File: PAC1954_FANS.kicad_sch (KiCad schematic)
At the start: 11 parts, among them U25 PAC1954T-E_4MX

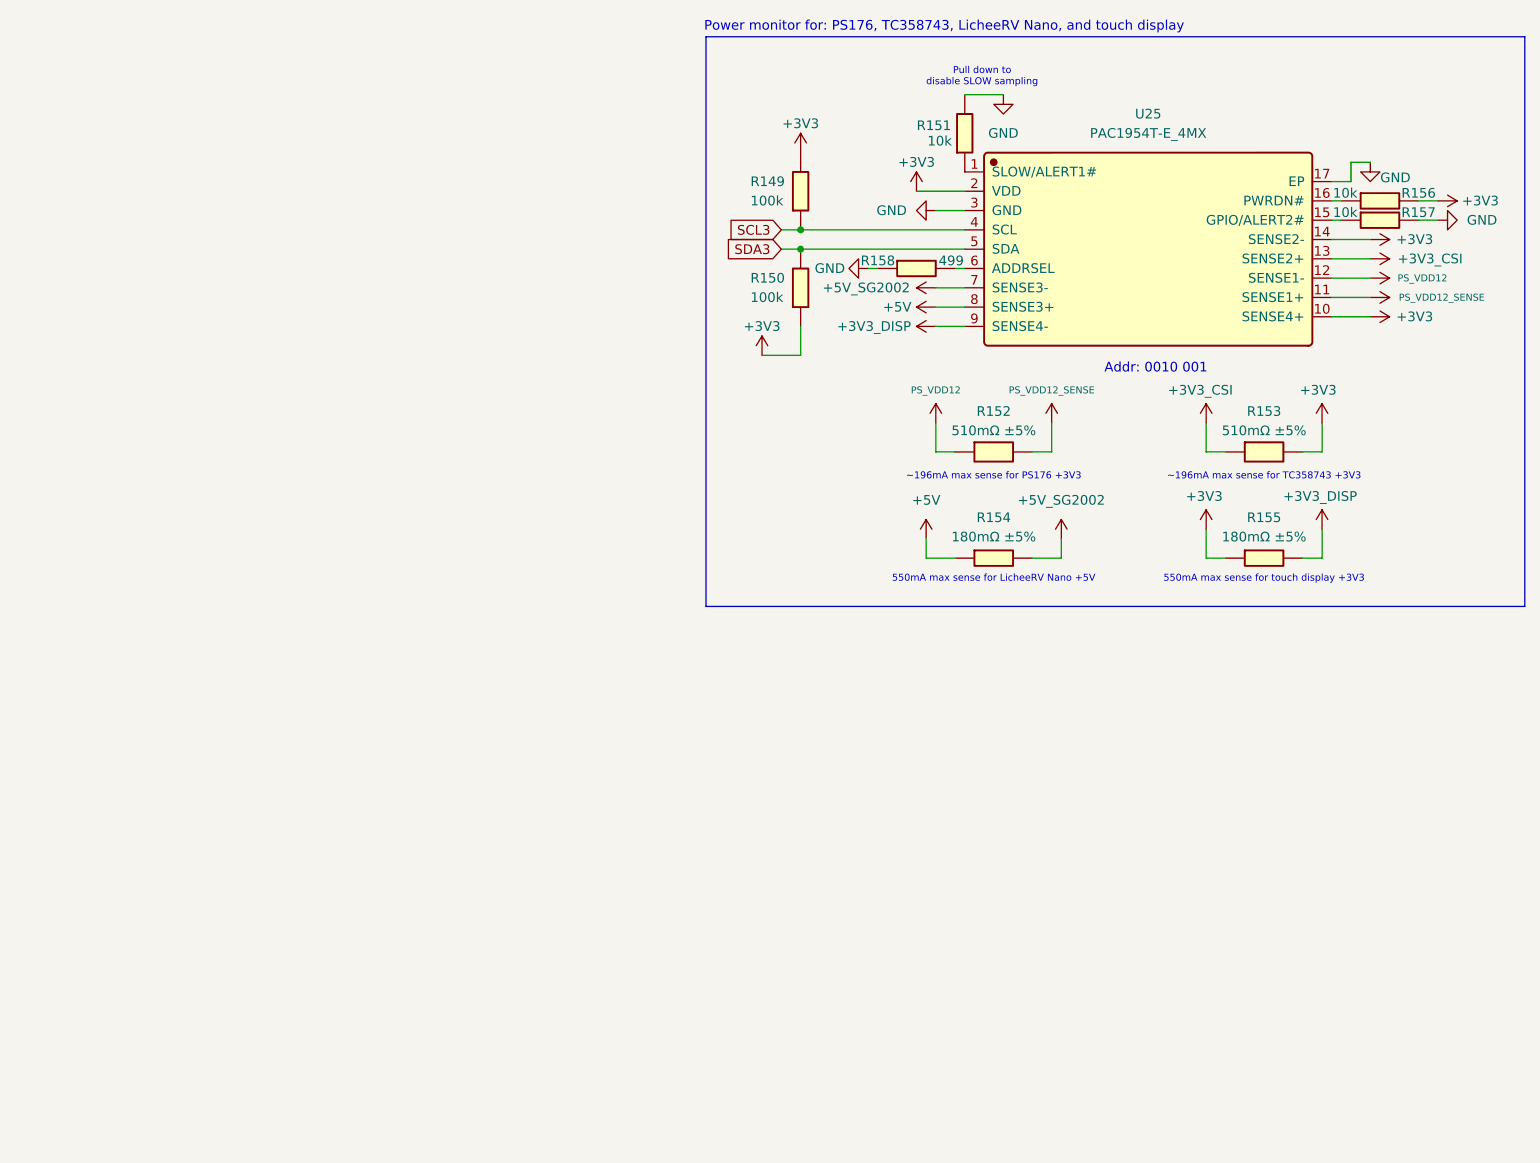
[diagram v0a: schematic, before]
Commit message: Mostly complete initial transfer to hierarchical schematic
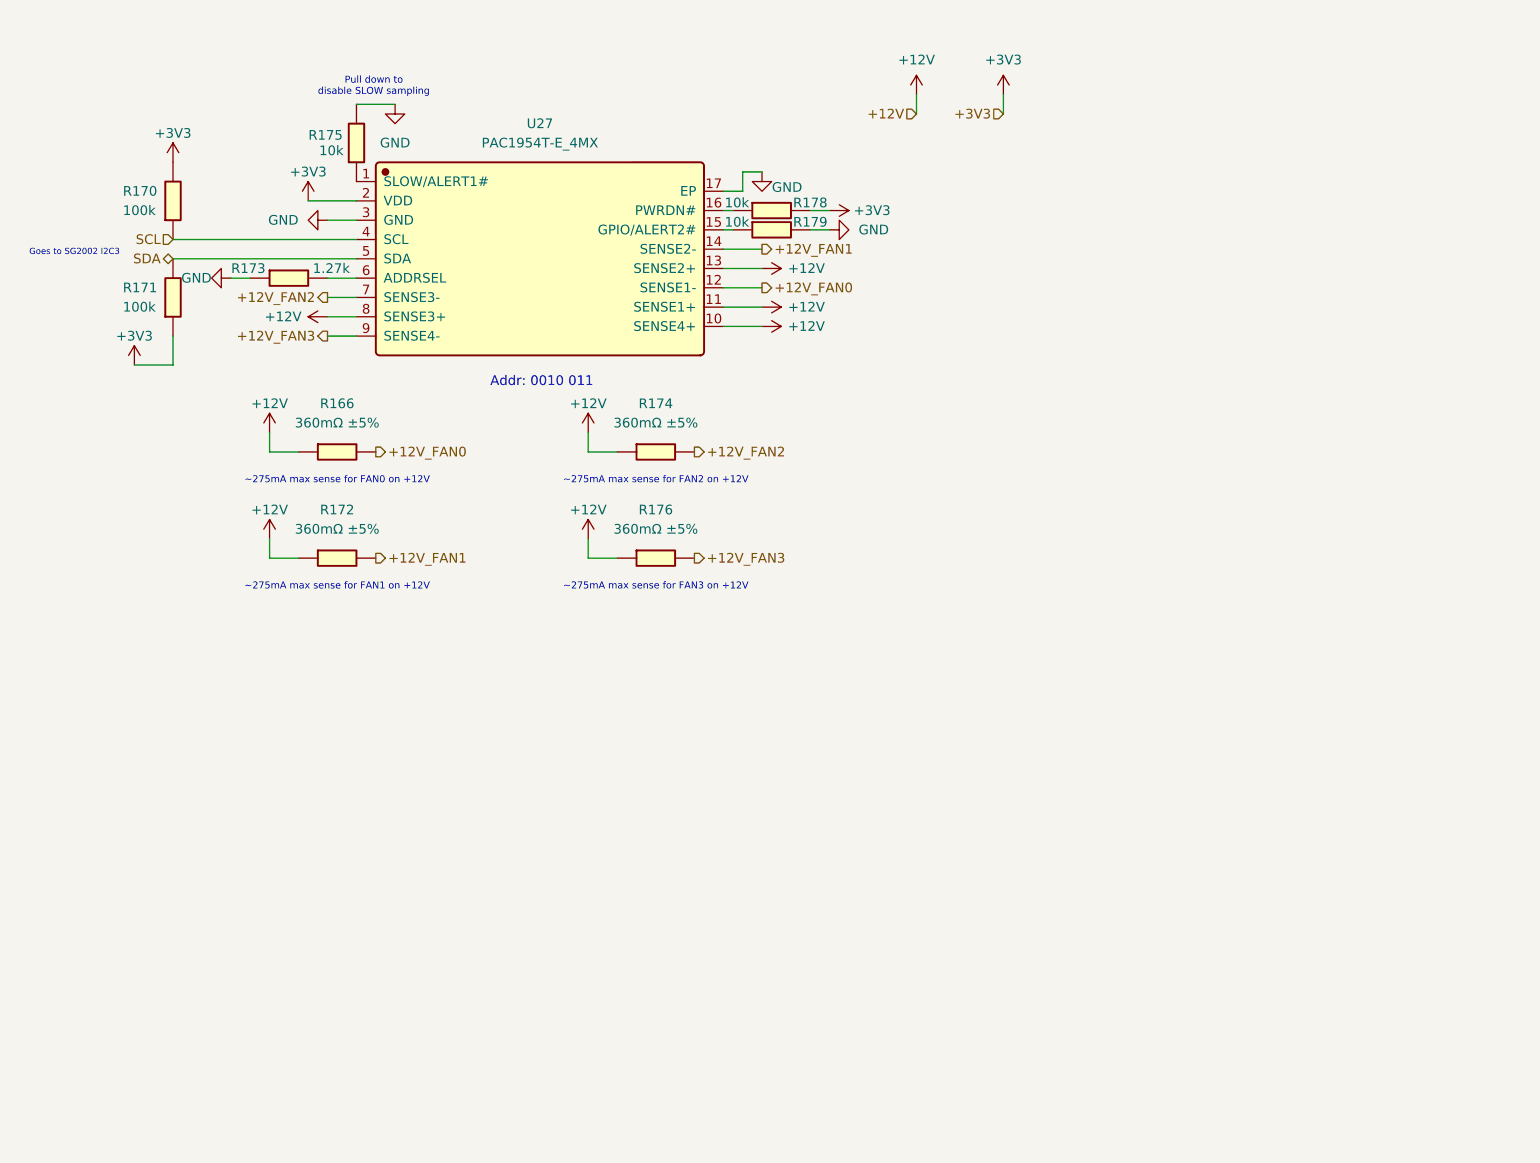
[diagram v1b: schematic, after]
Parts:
- removed R149, R150: 100k, Resistor_SMD:R_0402_1005Metric, symbol JLCImport:0402WGF1003TCE
- removed R151, R156, R157: 10k, Resistor_SMD:R_0402_1005Metric, symbol JLCImport:0402WGF1002TCE
- removed R152, R153: 510mΩ ±5%, Resistor_SMD:R_1210_3225Metric, symbol JLCImport:YHR1206SE1WR003F5
- removed R154, R155: 180mΩ ±5%, Resistor_SMD:R_0508_1220Metric, symbol JLCImport:LTR10EVHJLR18
- removed R158: 499, Resistor_SMD:R_0402_1005Metric, symbol JLCImport:WR04W1R00FTL
- removed U25: PAC1954T-E_4MX, JLCImport:PAC1954T-E_4MX, symbol JLCImport:PAC1954T-E_4MX
- added R166, R172, R174, R176: 360mΩ ±5%, Resistor_SMD:R_0805_2012Metric, symbol JLCImport:RTT05R36JTP
- added R170, R171: 100k, Resistor_SMD:R_0402_1005Metric, symbol JLCImport:0402WGF1003TCE
- added R173: 1.27k, Resistor_SMD:R_0402_1005Metric, symbol JLCImport:WR04X1271FTL
- added R175, R178, R179: 10k, Resistor_SMD:R_0402_1005Metric, symbol JLCImport:0402WGF1002TCE
- added U27: PAC1954T-E_4MX, JLCImport:PAC1954T-E_4MX, symbol JLCImport:PAC1954T-E_4MX
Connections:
- net +3V3: now also R170.2, R171.1, R178.2, U27.2 (VDD)
- net GND: now also R173.1, R175.2, R179.2, U27.17 (EP), U27.3 (GND)
- new net: R175.1, U27.1 (SLOW/ALERT1#)
- new net: R179.1, U27.15 (GPIO/ALERT2#)
- new net: R178.1, U27.16 (PWRDN#)
- new net: R173.2, U27.6 (ADDRSEL)
- new net +12V: R166.1, R172.1, R174.1, R176.1, U27.10 (SENSE4+), U27.11 (SENSE1+), U27.13 (SENSE2+), U27.8 (SENSE3+)
- new net +12V_FAN0: R166.2, U27.12 (SENSE1-)
- new net +12V_FAN1: R172.2, U27.14 (SENSE2-)
- new net +12V_FAN2: R174.2, U27.7 (SENSE3-)
- new net +12V_FAN3: R176.2, U27.9 (SENSE4-)
- new net SCL: R170.1, U27.4 (SCL)
- new net SDA: R171.2, U27.5 (SDA)
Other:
- note added: "Addr: 0010 011"
- note added: "Goes to SG2002 I2C3"
- note added: "~275mA max sense for FAN0 on +12V"
- note added: "~275mA max sense for FAN1 on +12V"
- note added: "~275mA max sense for FAN2 on +12V"
- note added: "~275mA max sense for FAN3 on +12V"
- note removed: "550mA max sense for LicheeRV Nano +5V"
- note removed: "550mA max sense for touch display +3V3"
- note removed: "Addr: 0010 001"
- note removed: "Power monitor for: PS176, TC358743, LicheeRV Nano, and touch display"
- note removed: "~196mA max sense for PS176 +3V3"
- note removed: "~196mA max sense for TC358743 +3V3"
- company: Designed by: Matthew Kong -> (none)
- title: Temperature and Power monitor sensors -> (none)

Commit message: Transferred everything to hierarchical schematic and wired PSU power on circuit AND created duplicate schematics for all relevant subsystems
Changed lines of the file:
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@@
+	(wire
+		(pts
+			(xy 96.5962 96.5962) (xy 110.5662 96.5962)
+		)
+		(stroke
+			(width 0)
+			(type default)
+		)
+	)
+	(wire
+		(pts
+			(xy 94.0562 166.4462) (xy 94.0562 94.0562)
+		)
+		(stroke
+			(width 0)
+			(type default)
+		)
+	)
 	(wire
 		(pts
@@
 	(wire
 		(pts
+			(xy 143.5862 166.4462) (xy 94.0562 166.4462)
+		)
+		(stroke
+			(width 0)
+			(type default)
+		)
+	)
+	(wire
+		(pts
+			(xy 96.5962 163.9062) (xy 96.5962 96.5962)
+		)
+		(stroke
+			(width 0)
+			(type default)
+		)
+	)
+	(wire
+		(pts
 			(xy 59.69 46.99) (xy 83.82 46.99)
 		)
@@
 	(wire
 		(pts
+			(xy 94.0562 94.0562) (xy 110.5662 94.0562)
+		)
+		(stroke
+			(width 0)
+			(type default)
+		)
+	)
+	(wire
+		(pts
 			(xy 133.35 43.18) (xy 132.08 43.18)
 		)
@@
 		)
 		(stroke
+			(width 0)
+			(type default)
+		)
+	)
+	(wire
+		(pts
+			(xy 141.0462 163.9062) (xy 96.5962 163.9062)
+		)
+		(stroke
